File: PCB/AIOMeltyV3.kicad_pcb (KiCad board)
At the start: 2 copper layers, 39.7 x 26.2 mm, 35 parts, among them J1 USB4500-03-0-A_REVA1, SW1 Boot, SW2 Reset, U3 ESP32-S3-MINI-1, U4 RT9161A-33GV

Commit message: updated PCB
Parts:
- removed R11: 10k, Capacitor_SMD:C_01005_0402Metric
- added C1: 100nf, Capacitor_SMD:C_0402_1005Metric, F.Cu at (166.5, 106.0)
- added C5: 100nf, Capacitor_SMD:C_0402_1005Metric, F.Cu at (161.7, 95.0)
- C1, C12, C13, C2, C3, C4, R1, R10, R2, R3, R4, R5, R6, R7, R8, R9: footprint Capacitor_SMD:C_01005_0402Metric -> Capacitor_SMD:C_0402_1005Metric
- H1: value PWM2 -> PWM1
- moved R4 0.81 mm to (151.8, 107.1)
- moved R3 0.80 mm to (155.3, 107.1)
- moved C13 0.66 mm to (170.6, 99.9), turned to 90 degrees
- moved R5 0.61 mm to (167.2, 99.4)
- moved R2 0.45 mm to (154.4, 106.6)
- moved C12 0.38 mm to (168.0, 101.8)
- moved R9 0.33 mm to (143.7, 94.5)
- moved R1 0.16 mm to (153.1, 106.6)
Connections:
- H1 pad 1: PWM1 -> (no net)
- H2 pad 1: PWM2 -> (no net)
- H4 pad 1: +5V -> (no net)
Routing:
- net GND: track 3.65 -> 11.9 mm, vias 28 -> 30
- net +3V3: track 75.9 -> 77.0 mm
- net SCL: track 19.9 -> 19.2 mm
- net Net-(J1-CC1): track 1.13 -> 1.76 mm
- net Net-(U3-EN): track 17.9 -> 18.5 mm
- net Net-(J1-CC2): track 1.22 -> 1.80 mm
- net USB_P: track 2.15 -> 1.57 mm

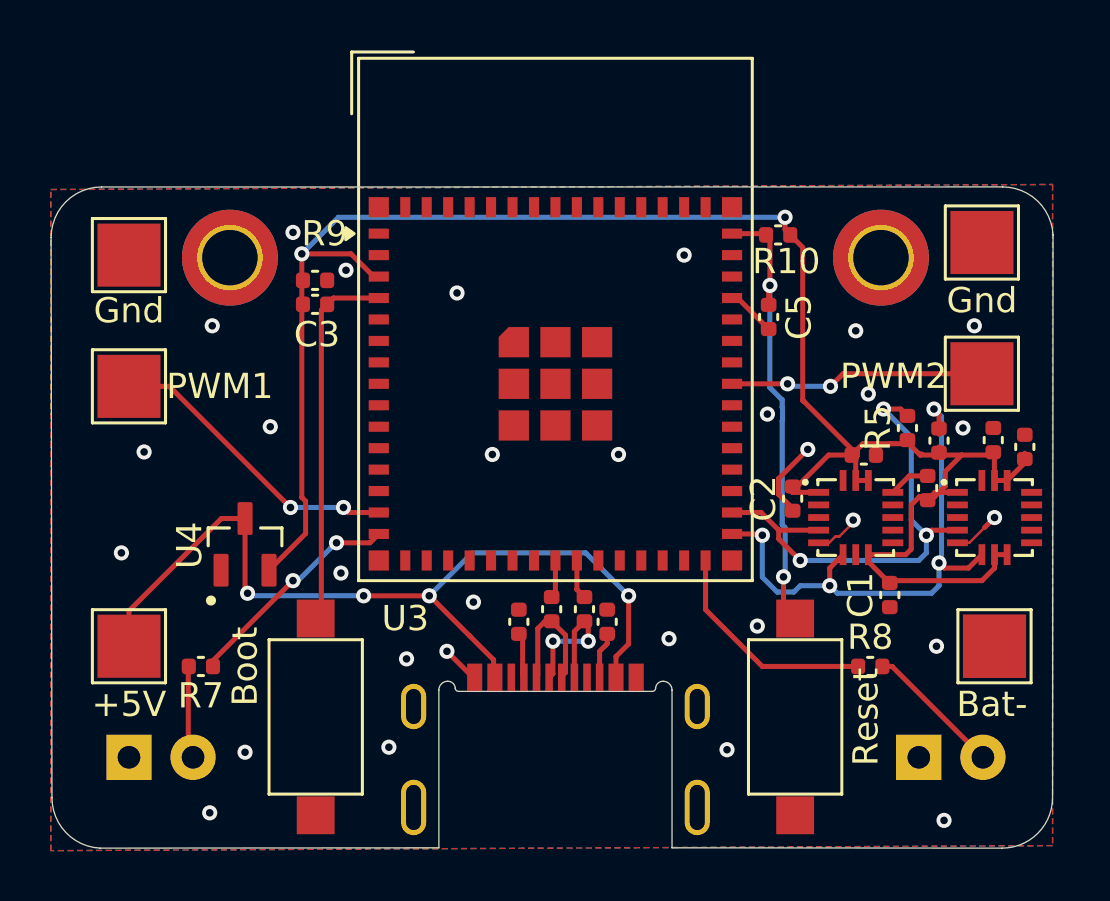
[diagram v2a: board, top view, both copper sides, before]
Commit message: Robot moves, I2C should now be on the correct pins
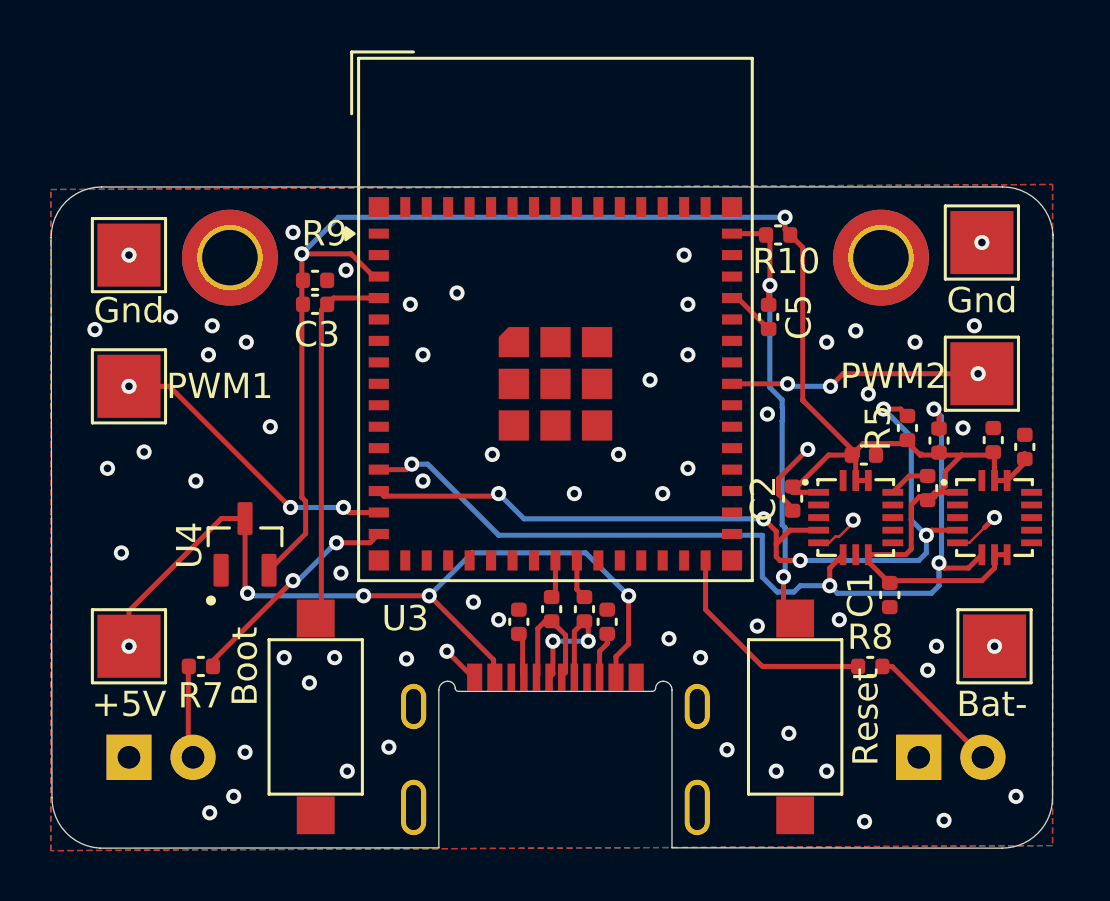
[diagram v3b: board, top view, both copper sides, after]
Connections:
- H3 pad 1: GND -> (no net)
- U3 pad 12: unconnected-(U3-IO8-Pad12) -> SDA
- U3 pad 13: unconnected-(U3-IO9-Pad13) -> SCL
- U3 pad 31: SDA -> unconnected-(U3-IO35-Pad31)
- U3 pad 32: SCL -> unconnected-(U3-IO36-Pad32)
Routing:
- net SDA: track 22.2 -> 37.6 mm
- net SCL: track 19.2 -> 34.3 mm, vias 3 -> 5
- net PWM2: vias 2 -> 3
- net PWM1: vias 2 -> 3
- net GND: vias 30 -> 63
- net +5V: vias 4 -> 5
- net (no net): vias 0 -> 1

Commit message: updated PCB I2C
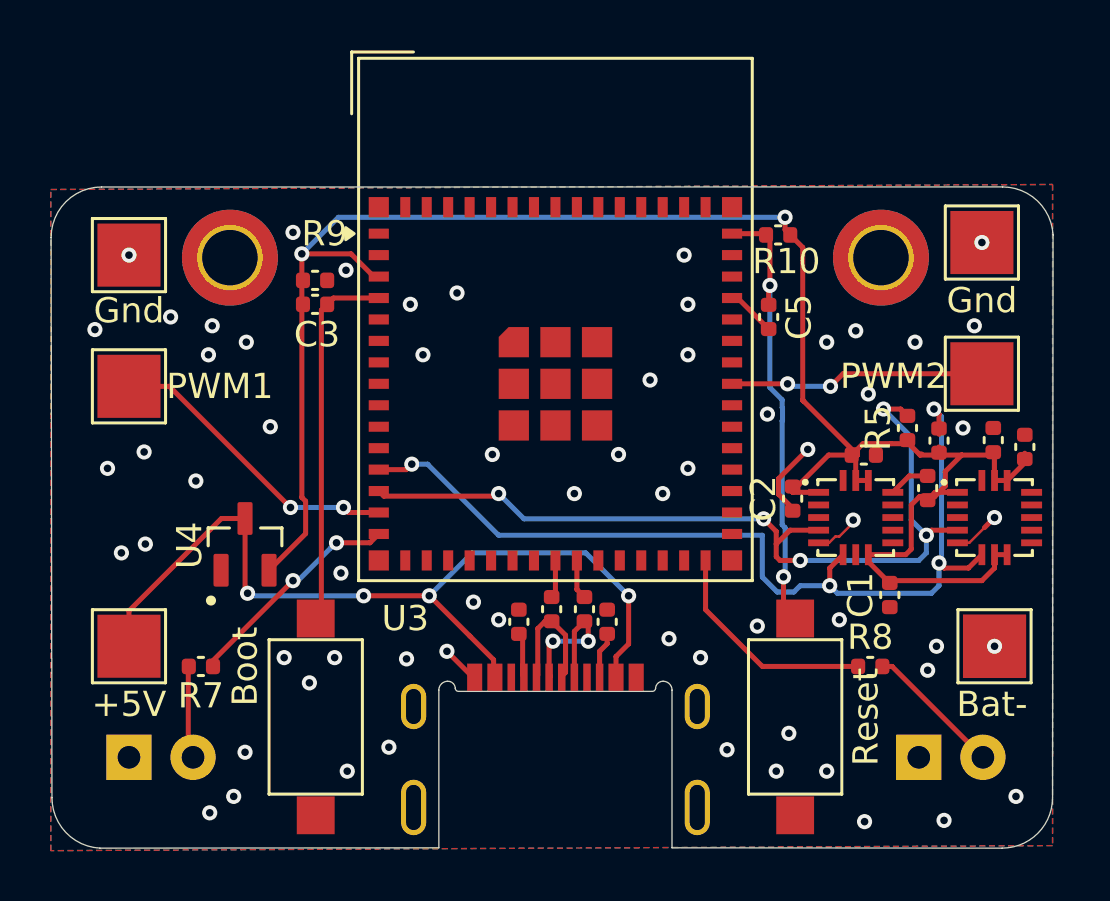
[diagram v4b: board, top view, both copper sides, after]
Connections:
- H3 pad 1: (no net) -> GND
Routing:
- net PWM2: vias 3 -> 2
- net PWM1: vias 3 -> 2
- net GND: vias 63 -> 64
- net +5V: vias 5 -> 4
- net (no net): vias 1 -> 0
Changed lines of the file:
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@@
 			(size 2.5 2.5)
 			(layers "F.Cu" "F.Mask")
+			(net 2 "GND")
 		)
 		(embedded_fonts no)
@@
 		)
 	)
-	(via
-		(at 170.15 92.05)
-		(size 0.6)
-		(drill 0.3)
-		(layers "F.Cu" "B.Cu")
-		(net 0)
-	)
 	(segment
 		(start 168.275 102.125)
@@
 	)
 	(via
+		(at 170.15 92.05)
+		(size 0.6)
+		(drill 0.3)
+		(layers "F.Cu" "B.Cu")
+		(net 2)
+	)
+	(via
 		(at 142.85 91.65)
 		(size 0.6)
@@
 	)
 	(via
-		(at 148 101.5)
+		(at 137 104)
 		(size 0.6)
 		(drill 0.3)
@@
 	)
 	(via
-		(at 136.35 108.05)
-		(size 0.6)
-		(drill 0.3)
-		(layers "F.Cu" "B.Cu")
-		(net 3)
-	)
-	(via
 		(at 156.15 106.05)
 		(size 0.6)
@@
 	)
 	(segment
-		(start 153.05 109.2375)
-		(end 153 109.2375)
+		(start 153 109.1875)
+		(end 153.05 109.2375)
 		(width 0.2)
 		(layer "F.Cu")
@@
 	)
 	(segment
-		(start 153.15 107.85)
-		(end 153.15 109.1375)
+		(start 153 108)
+		(end 153 109.1875)
 		(width 0.2)
 		(layer "F.Cu")
@@
 	)
 	(segment
-		(start 153.15 109.1375)
-		(end 153.05 109.2375)
+		(start 153.05 109.2375)
+		(end 153 109.2375)
+		(width 0.2)
+		(layer "F.Cu")
+		(net 11)
+	)
+	(segment
+		(start 153.15 107.85)
+		(end 153 108)
 		(width 0.2)
 		(layer "F.Cu")
@@
 	)
 	(segment
-		(start 153.65 109.0875)
-		(end 153.5 109.2375)
+		(start 152.55 107.35)
+		(end 152.84 107.06)
 		(width 0.2)
 		(layer "F.Cu")
@@
 	)
 	(segment
-		(start 153.65 107.61)
-		(end 153.65 109.0875)
+		(start 153.65 109.0875)
+		(end 153.5 109.2375)
 		(width 0.2)
 		(layer "F.Cu")
@@
 	)
 	(segment
-		(start 152.55 107.35)
-		(end 152.84 107.06)
+		(start 152.5 109.2375)
+		(end 152.55 109.1875)
 		(width 0.2)
 		(layer "F.Cu")
@@
 	)
 	(segment
-		(start 152.5 109.2375)
-		(end 152.55 109.1875)
+		(start 153.1 107.06)
+		(end 153.65 107.61)
 		(width 0.2)
 		(layer "F.Cu")
@@
 	)
 	(segment
-		(start 153.1 107.06)
-		(end 153.65 107.61)
+		(start 152.84 107.06)
+		(end 153.1 107.06)
 		(width 0.2)
 		(layer "F.Cu")
@@
 	)
 	(segment
-		(start 152.84 107.06)
-		(end 153.1 107.06)
+		(start 153.65 107.61)
+		(end 153.65 109.0875)
 		(width 0.2)
 		(layer "F.Cu")
@@
 		(net 50)
 	)
-	(via
-		(at 136.35 97.75)
-		(size 0.6)
-		(drill 0.3)
-		(layers "F.Cu" "B.Cu")
-		(net 50)
-	)
 	(segment
 		(start 144.85 102.55)
@@
 		(net 51)
 	)
-	(via
-		(at 170 97.25)
-		(size 0.6)
-		(drill 0.3)
-		(layers "F.Cu" "B.Cu")
-		(net 51)
-	)
